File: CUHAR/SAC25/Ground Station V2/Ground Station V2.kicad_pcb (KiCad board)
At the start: 2 copper layers, 51.5 x 28.3 mm, 38 parts, among them J1 Connector, USB-TYPE-C-16P, J3 Conn_Coaxial, SW1 SW_Push, SW2 SW_Push, U1 ESP32-S3, U2 USBLC6-2P6, U3 W25Q128, U4 AMS1117, X1 40MHz, 15pF

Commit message: forgor to commit
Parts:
- added G***: LOGO, LOGO, B.Cu at (128.5, 107.6)
- added J2: Conn_01x19_Pin, Connector_PinSocket_2.54mm:PinSocket_1x19_P2.54mm_Vertical, F.Cu at (114.3, 94.9)
- added J4: Conn_01x19_Pin, Connector_PinSocket_2.54mm:PinSocket_1x19_P2.54mm_Vertical, F.Cu at (114.3, 120.3)
- C14, C15: value 22uF -> 10uF
- moved C14 32.8 mm to (122.6, 115.2), turned to -90 degrees
- moved R4 32.4 mm to (124.7, 110.3)
- moved C2 32.0 mm to (152.9, 113.3), turned to 0 degrees
- moved D2 31.4 mm to (120.1, 115.2), turned to -90 degrees
- moved D3 30.5 mm to (122.4, 111.3)
- moved C15 30.0 mm to (131.2, 110.0)
- moved U4 30.0 mm to (128.2, 114.4)
- moved C9 26.4 mm to (152.9, 115.1), turned to 0 degrees
- moved C6 24.5 mm to (141.2, 105.1)
- moved D1 24.1 mm to (120.1, 111.0), turned to 90 degrees
- moved C3 23.1 mm to (156.8, 106.2), turned to 90 degrees
- moved C16 23.0 mm to (151.0, 117.3)
- moved C11 22.2 mm to (152.9, 114.2)
- moved C5 21.9 mm to (156.0, 106.2), turned to 90 degrees
- moved R3 21.8 mm to (133.6, 105.3), turned to -90 degrees
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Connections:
- U1 pad 13: /SDA -> /IO8
- U1 pad 14: /SCL -> /IO9
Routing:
- net GND: track 11.3 -> 68.3 mm, vias 57 -> 49
- net +3.3V: track 75.8 -> 116.3 mm, vias 6 -> 4
- net /IO21: track 0.00 -> 31.1 mm, vias 0 -> 2
- net /IO18: track 0.00 -> 30.3 mm
- net /IO17: track 0.00 -> 28.2 mm
- net /IO14: track 0.00 -> 27.3 mm
- net /RESET: track 45.3 -> 70.7 mm, vias 2 -> 3
- net /IO13: track 0.00 -> 25.2 mm
- net /IO33: track 0.00 -> 25.0 mm
- net /IO12: track 0.00 -> 23.1 mm
- net /IO34: track 0.00 -> 22.3 mm
- net /IO1: track 0.00 -> 21.7 mm
- net /IO11: track 0.00 -> 21.0 mm
- net /IO35: track 0.00 -> 19.6 mm
- net /IO2: track 0.00 -> 19.0 mm
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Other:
- outline, holes or cut-outs redrawn
- board text added: "3V3"
- board text added: "BOOT"
- board text added: "By: Boonyakorn Tanrattanakorn"
- board text added: "CUHAR ESP32 DEVKIT V1.0"
- board text added: "D1"
- board text added: "D10"
- board text added: "D11"
- board text added: "D12"
- board text added: "D13"
- board text added: "D14"
- board text added: "D17"
- board text added: "D18"
- board text added: "D2"
- board text added: "D21"
- board text added: "D3"
- board text added: "D33"
- board text added: "D34"
- board text added: "D35"
- board text added: "D36"
- board text added: "D37"
- board text added: "D38"
- board text added: "D4"
- board text added: "D45"
- board text added: "D46"
- board text added: "D5"
- board text added: "D6"
- board text added: "D7"
- board text added: "D8"
- board text added: "D9"
- board text added: "EN"
- board text added: "GND"
- board text added: "RX0"
- board text added: "TCK"
- board text added: "TDI"
- board text added: "TDO"
- board text added: "TMS"
- board text added: "TX0"
- board text added: "VIN"

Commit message: some minor update
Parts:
- added R7: 510Ω, JLCPCB-Kicad-Footprints:R_0402, F.Cu at (145.4, 117.1)
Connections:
- U1 pad 49: /U0TXD -> Net-(U1-U0TXD)
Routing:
- net /U0TXD: track 9.07 -> 3.52 mm
- net Net-(U1-U0TXD): track 0.00 -> 4.77 mm

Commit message: Added via stitching
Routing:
- net GND: vias 49 -> 68
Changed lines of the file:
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@@
 	)
 	(via
+		(at 160.865716 116.616952)
+		(size 0.6)
+		(drill 0.3)
+		(layers "F.Cu" "B.Cu")
+		(free yes)
+		(net 2)
+	)
+	(via
 		(at 125.603 109.145)
 		(size 0.6)
@@
 	)
 	(via
+		(at 153.245716 101.376952)
+		(size 0.6)
+		(drill 0.3)
+		(layers "F.Cu" "B.Cu")
+		(free yes)
+		(net 2)
+	)
+	(via
 		(at 124.841 108.383)
 		(size 0.6)
@@
 	)
 	(via
+		(at 132.925716 111.536952)
+		(size 0.6)
+		(drill 0.3)
+		(layers "F.Cu" "B.Cu")
+		(free yes)
+		(net 2)
+	)
+	(via
 		(at 160.528 101.779)
 		(size 0.6)
@@
 	)
 	(via
+		(at 160.865716 98.836952)
+		(size 0.6)
+		(drill 0.3)
+		(layers "F.Cu" "B.Cu")
+		(free yes)
+		(net 2)
+	)
+	(via
+		(at 127.845716 106.456952)
+		(size 0.6)
+		(drill 0.3)
+		(layers "F.Cu" "B.Cu")
+		(free yes)
+		(net 2)
+	)
+	(via
 		(at 117.729 117.527)
 		(size 0.6)
@@
 	)
 	(via
+		(at 125.305716 103.916952)
+		(size 0.6)
+		(drill 0.3)
+		(layers "F.Cu" "B.Cu")
+		(free yes)
+		(net 2)
+	)
+	(via
 		(at 119.126 104.573)
 		(size 0.6)
@@
 	)
 	(via
+		(at 155.785716 98.836952)
+		(size 0.6)
+		(drill 0.3)
+		(layers "F.Cu" "B.Cu")
+		(free yes)
+		(net 2)
+	)
+	(via
 		(at 112.522 98.223)
 		(size 0.6)
@@
 	)
 	(via
+		(at 158.325716 114.076952)
+		(size 0.6)
+		(drill 0.3)
+		(layers "F.Cu" "B.Cu")
+		(free yes)
+		(net 2)
+	)
+	(via
 		(at 119.126 111.685)
 		(size 0.6)
@@
 	)
 	(via
+		(at 158.325716 98.836952)
+		(size 0.6)
+		(drill 0.3)
+		(layers "F.Cu" "B.Cu")
+		(free yes)
+		(net 2)
+	)
+	(via
 		(at 131.1656 107.2146)
 		(size 0.6)
@@
 	)
 	(via
+		(at 122.765716 103.916952)
+		(size 0.6)
+		(drill 0.3)
+		(layers "F.Cu" "B.Cu")
+		(free yes)
+		(net 2)
+	)
+	(via
 		(at 119.888 110.923)
 		(size 0.6)
@@
 	)
 	(via
+		(at 155.785716 101.376952)
+		(size 0.6)
+		(drill 0.3)
+		(layers "F.Cu" "B.Cu")
+		(free yes)
+		(net 2)
+	)
+	(via
 		(at 129.7432 108.6878)
 		(size 0.6)
@@
 	)
 	(via
+		(at 127.845716 108.996952)
+		(size 0.6)
+		(drill 0.3)
+		(layers "F.Cu" "B.Cu")
+		(free yes)
+		(net 2)
+	)
+	(via
 		(at 146.177 101.525)
 		(size 0.6)
@@
 	)
 	(via
+		(at 155.785716 103.916952)
+		(size 0.6)
+		(drill 0.3)
+		(layers "F.Cu" "B.Cu")
+		(free yes)
+		(net 2)
+	)
+	(via
 		(at 112.522 120.321)
 		(size 0.6)
@@
 	)
 	(via
+		(at 127.845716 111.536952)
+		(size 0.6)
+		(drill 0.3)
+		(layers "F.Cu" "B.Cu")
+		(free yes)
+		(net 2)
+	)
+	(via
 		(at 154.178 109.399)
 		(size 0.6)
@@
 	)
 	(via
+		(at 130.385716 103.916952)
+		(size 0.6)
+		(drill 0.3)
+		(layers "F.Cu" "B.Cu")
+		(free yes)
+		(net 2)
+	)
+	(via
+		(at 155.785716 116.616952)
+		(size 0.6)
+		(drill 0.3)
+		(layers "F.Cu" "B.Cu")
+		(free yes)
+		(net 2)
+	)
+	(via
 		(at 120.142 115.622)
 		(size 0.6)
@@
 	)
 	(via
+		(at 158.325716 101.376952)
+		(size 0.6)
+		(drill 0.3)
+		(layers "F.Cu" "B.Cu")
+		(free yes)
+		(net 2)
+	)
+	(via
 		(at 139.5984 110.415)
 		(size 0.6)
@@
 	)
 	(via
+		(at 112.605716 96.296952)
+		(size 0.6)
+		(drill 0.3)
+		(layers "F.Cu" "B.Cu")
+		(free yes)
+		(net 2)
+	)
+	(via
+		(at 120.225716 98.836952)
+		(size 0.6)
+		(drill 0.3)
+		(layers "F.Cu" "B.Cu")
+		(free yes)
+		(net 2)
+	)
+	(via
 		(at 160.528 113.463)
 		(size 0.6)
@@
 	)
 	(segment
-		(start 138.523 107.079)
-		(end 142.432 107.079)
+		(start 134.991 107.222)
+		(end 133.604 105.835)
 		(width 0.2)
 		(layer "F.Cu")
@@
 	)
 	(segment
-		(start 134.991 110.389)
-		(end 134.991 107.222)
+		(start 138.523 107.079)
+		(end 142.432 107.079)
 		(width 0.2)
 		(layer "F.Cu")
@@
 	)
 	(segment
-		(start 134.991 107.222)
-		(end 133.604 105.835)
+		(start 134.991 110.389)
+		(end 134.991 107.222)
 		(width 0.2)
 		(layer "F.Cu")
@@
 	(segment
 		(start 134.991 109.917)
-		(end 134.991 110.389)
+		(end 138.176 106.732)
 		(width 0.2)
 		(layer "B.Cu")
@@
 	)
 	(segment
-		(start 138.176 106.732)
+		(start 134.991 110.389)
 		(end 134.991 109.917)
 		(width 0.2)
@@
 		)
 	)
+	(group "ViaStitching GND"
+		(members "08c0dc61-4c7e-457c-a1c5-b3515deb81fc" "0b7df33d-4a9b-4baa-b04e-015f9e4a2a05"
+			"1a3655c2-fc75-4e55-952b-3f0aa7d7e6a4" "2280d4d2-cf6e-4eae-aa2f-640f110ef0ea"
+			"25f0480c-27bb-4a4f-ad6a-1570d425c41c" "2a00b232-8e98-4e92-aeb8-3726b84d6df7"
+			"2e2d665d-ceca-4b1d-9e61-0f3470a1fc93" "810a5b48-d24f-4e30-b0af-cf4d82e59293"
+			"88fcf2d8-4487-49f7-8ebd-5bb0818a6d30" "94a76488-d781-425c-b580-70ecbac9710d"
+			"a142ab7f-38ab-4945-ae36-7aea4d25276d" "ac0968ac-957b-4771-a873-64e6556ab6db"
+			"b962aa20-853f-4cfe-b655-b3ea2d28dd63" "ca1099ca-e141-4a5d-bdcc-6f26366c6ff7"
+			"cd73e72c-7dfc-4e31-92f2-a25c40172591" "cd9fa900-ddce-4b56-ae51-0327e2d39fd9"
+			"d7175b43-4897-4f0a-a70f-91ac6188e5f3" "e4403552-9a5b-41b3-ba73-b8d1d4a792d6"
+			"ec70a873-c007-45d4-8230-98e5d778a6a7"
+		)
+	)

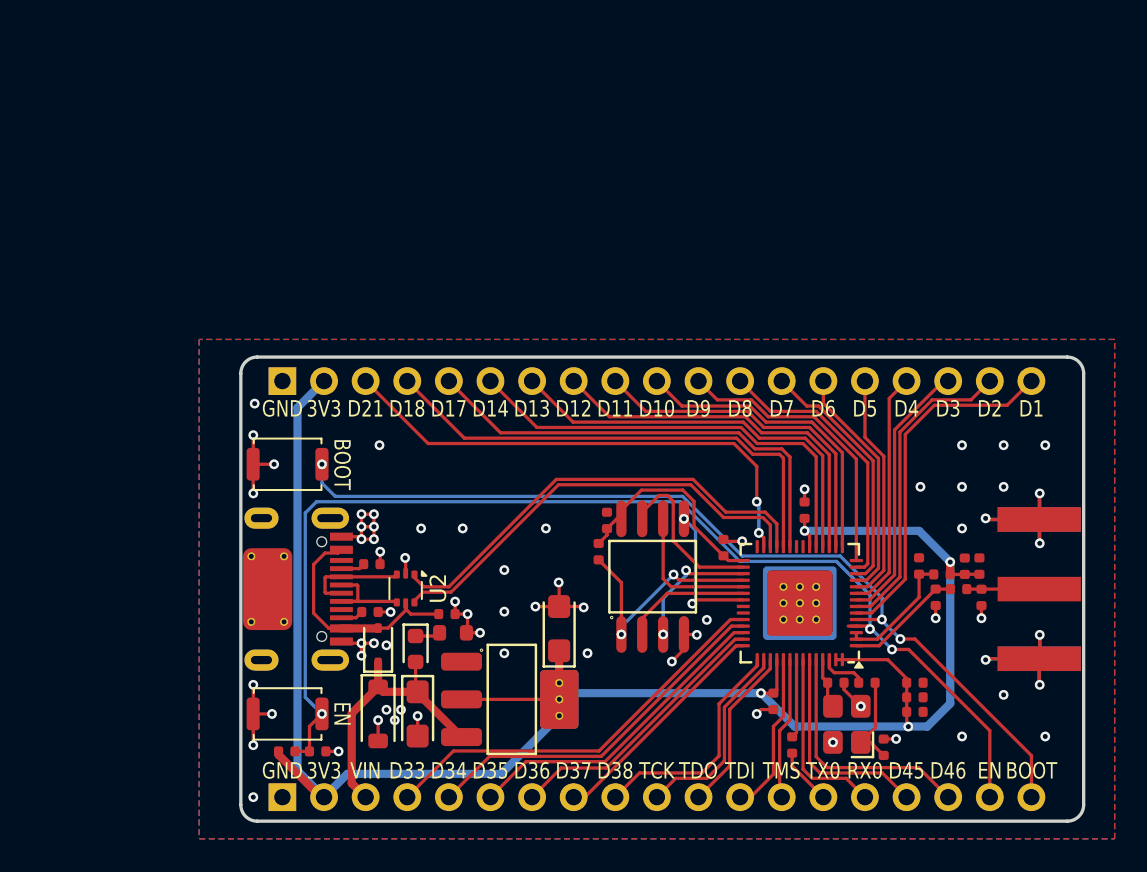
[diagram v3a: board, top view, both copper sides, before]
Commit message: fillet trace
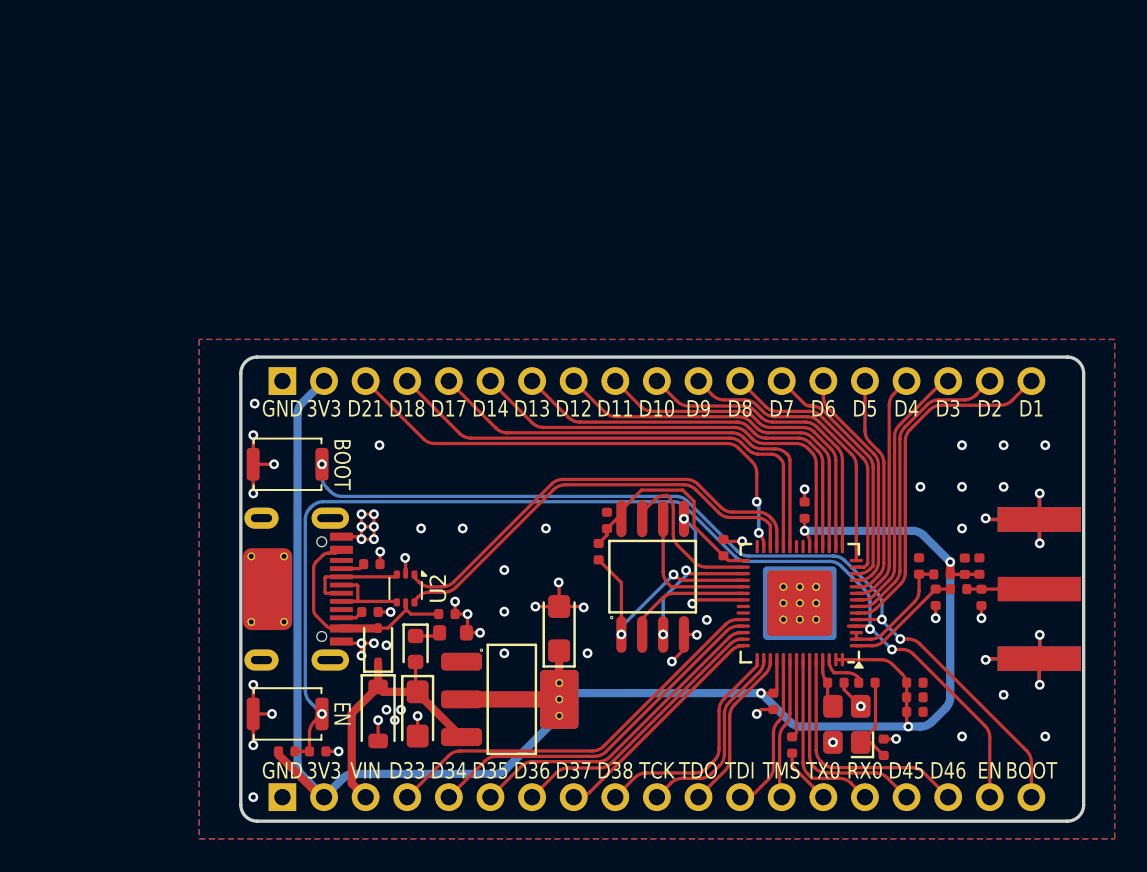
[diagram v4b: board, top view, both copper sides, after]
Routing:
- net +3.3V: track 116.3 -> 115.7 mm
